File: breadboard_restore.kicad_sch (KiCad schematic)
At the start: 10 parts, among them J1 黑 j列, J2 黑 j列, J3 黃 d列, J4 黃 c列, U1 nice!nano 相容 nRF52840, U2 WeAct BlackPill STM32F401/F411, U3 3.3V LDO（依接法推斷）, U4 BlackPill SWD 排孔

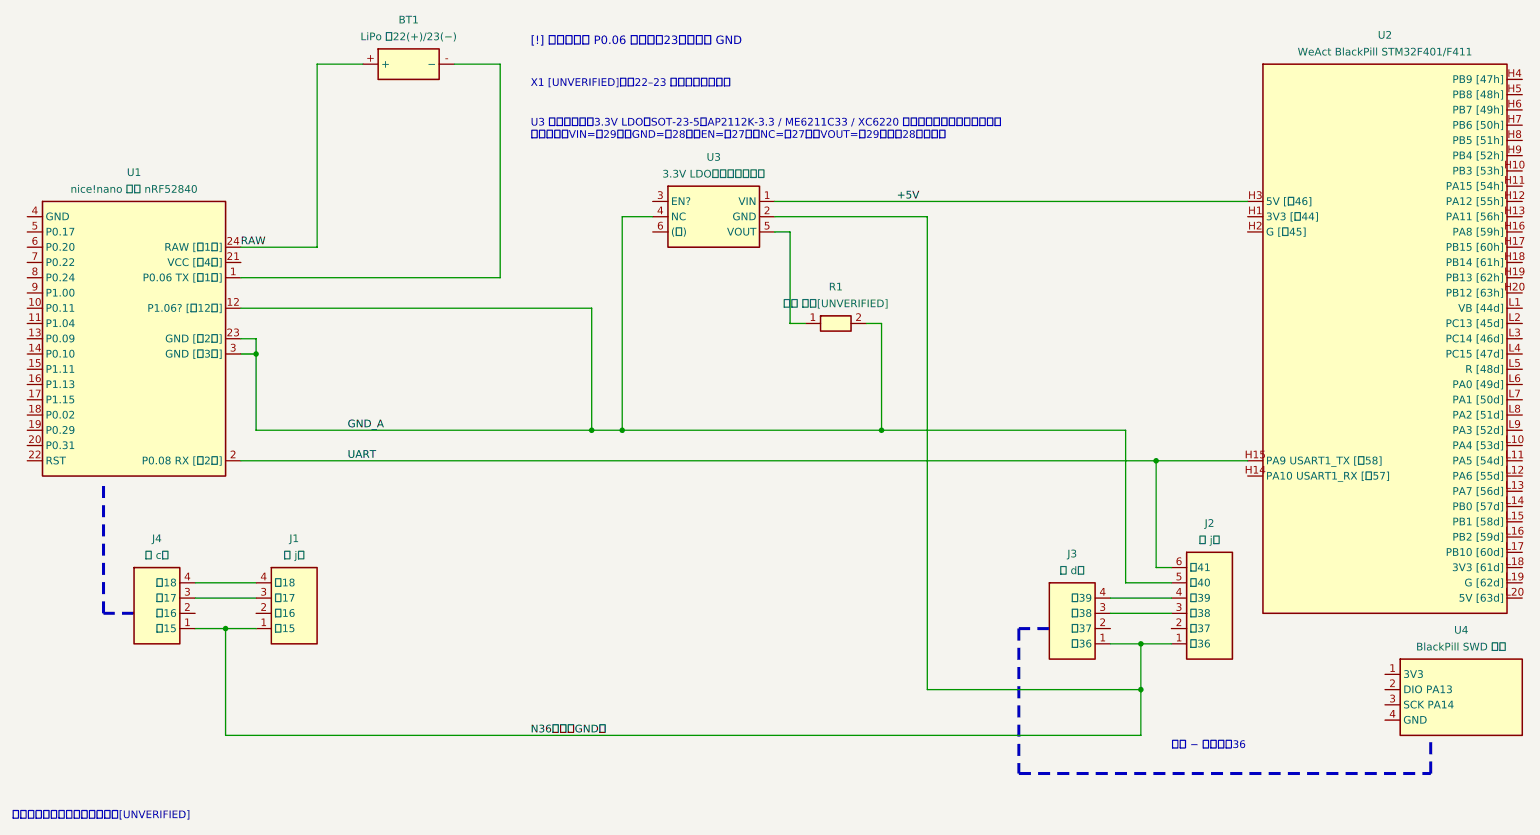
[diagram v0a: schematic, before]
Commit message: Correct wiring from annotated photos and identify U3 as DMC2038LVT
- Green GND wire lands on column 28 lower; add 27-top to 29-bottom link
- Fix long yellow P0.06 wire that never rendered (tube frame collapse)
- Purple wire no longer hidden under the red one
- Relabel U3 as DMC2038LVT complementary MOSFET in all figures and README

Co-Authored-By: Claude Opus 5.5 <noreply@anthropic.com>
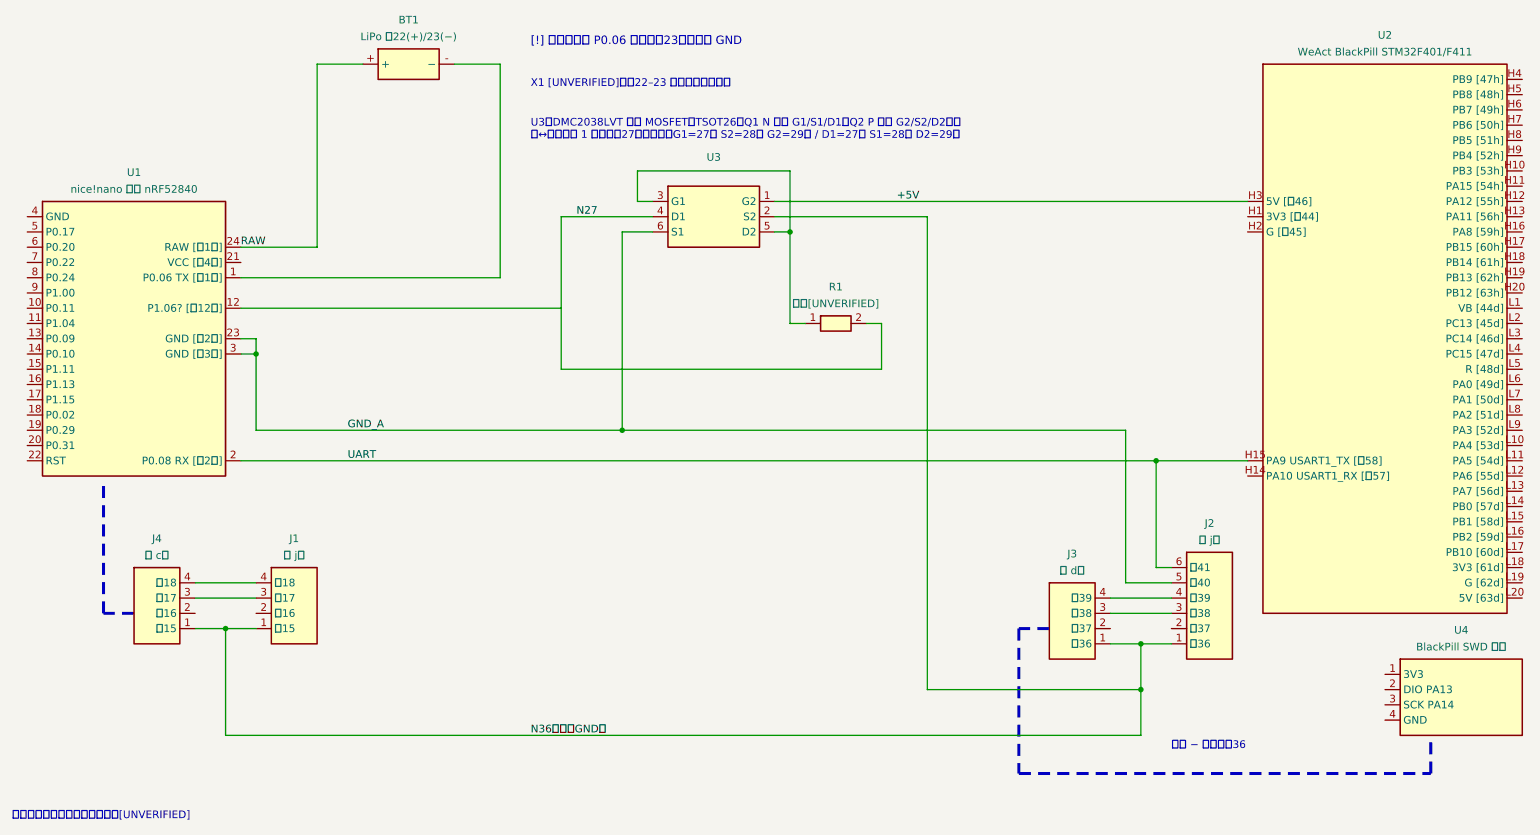
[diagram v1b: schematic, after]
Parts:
- removed U3: 3.3V LDO（依接法推斷）, symbol restore:U3_LDO_3V3_SOT23-5
- added U3: (no value), symbol restore:U3_DMC2038LVT
- R1: value 負載 阻值[UNVERIFIED] -> 阻值[UNVERIFIED]
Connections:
- net +5V: now also U3.1 (G2)
- net GND_A: now also U3.6 (S1); no longer R1.2, U1.12 (P1.06? [欄12下])
- net N36（推論GND）: now also U3.2 (S2)
- net at R1.1: now also U3.3 (G1), U3.5 (D2)
- new net N27: R1.2, U1.12 (P1.06? [欄12下]), U3.4 (D1)
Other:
- note added: "U3：DMC2038LVT 互補 MOSFET（TSOT26；Q1 N 通道 G1/S1/D1、Q2 P 通道 G2/S2/D2）。 腳↔欄位（依 1 號腳在欄27上推定）：G1=27上 S2=28上 G2=29上 / D1=27下 S1=28下 D2=29下"
- note removed: "U3 依接法推斷：3.3V LDO（SOT-23-5，AP2112K-3.3 / ME6211C33 / XC6220 同腳位），非讀取晶片字樣。 腳位對應：VIN=欄29上、GND=欄28上、EN=欄27上、NC=欄27下、VOUT=欄29下、欄28下無腳。"
